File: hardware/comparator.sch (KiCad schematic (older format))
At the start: 16 parts, among them U401 ADCMP580, U402 SY89321L

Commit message: added picture of assembled pcb, started erratum for r0..
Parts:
- R408: value JMP -> DNI
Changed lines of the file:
@@
 P 5700 4500
 F 0 "R408" V 5800 4550 50  0000 L CNN
-F 1 "JMP" V 5800 4350 50  0000 L CNN
+F 1 "DNI" V 5800 4350 50  0000 L CNN
 F 2 "Resistors_SMD:R_0402" H 5700 4500 50  0001 C CNN
 F 3 "~" H 5700 4500 50  0001 C CNN

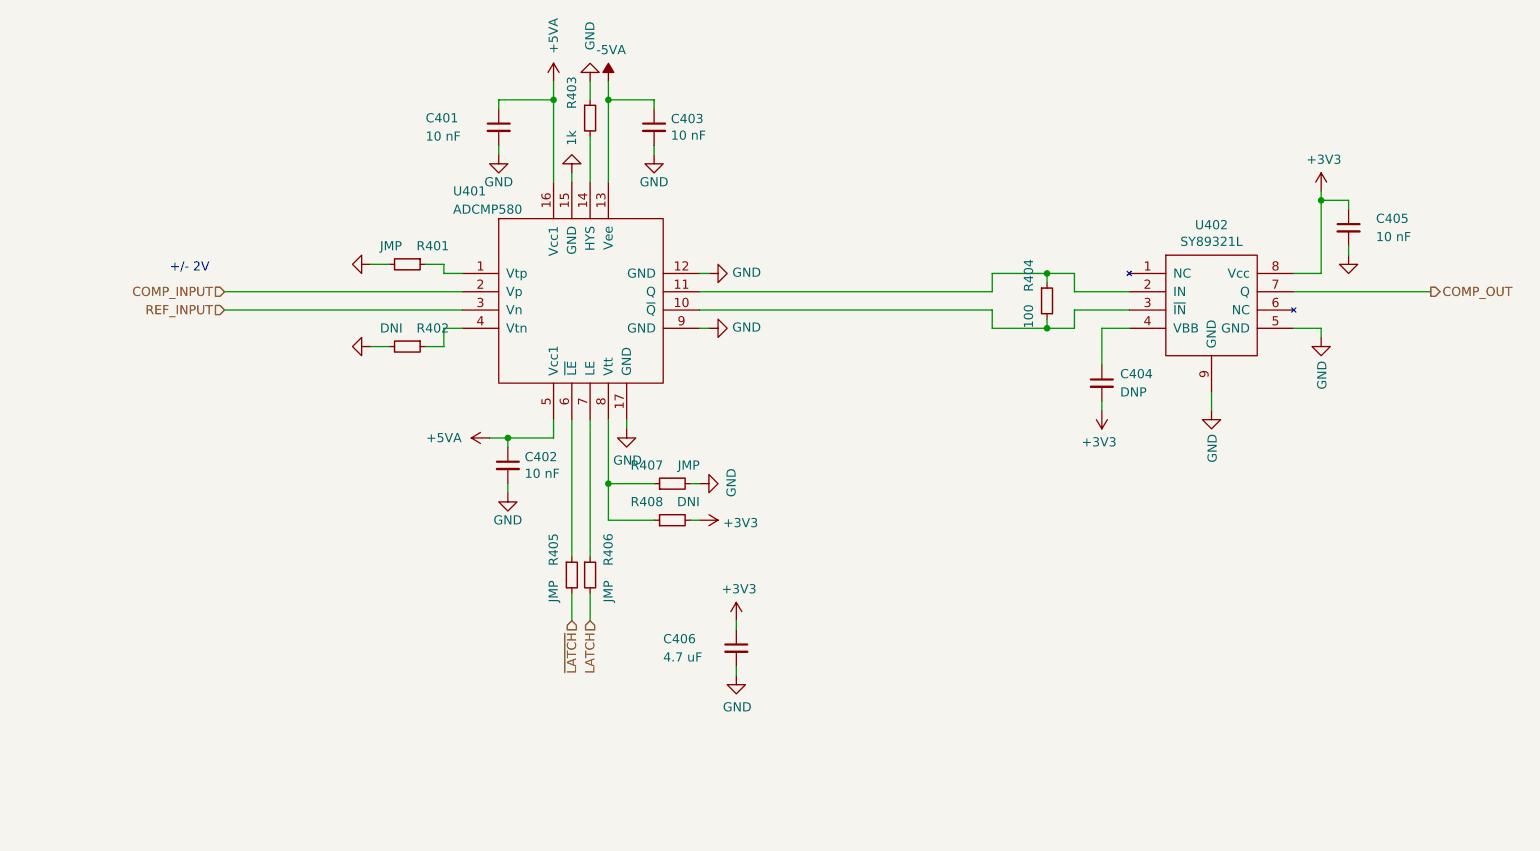
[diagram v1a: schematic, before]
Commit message: fixed U401 and U601 output termination, tdr works, added first sweep of output pulse to README
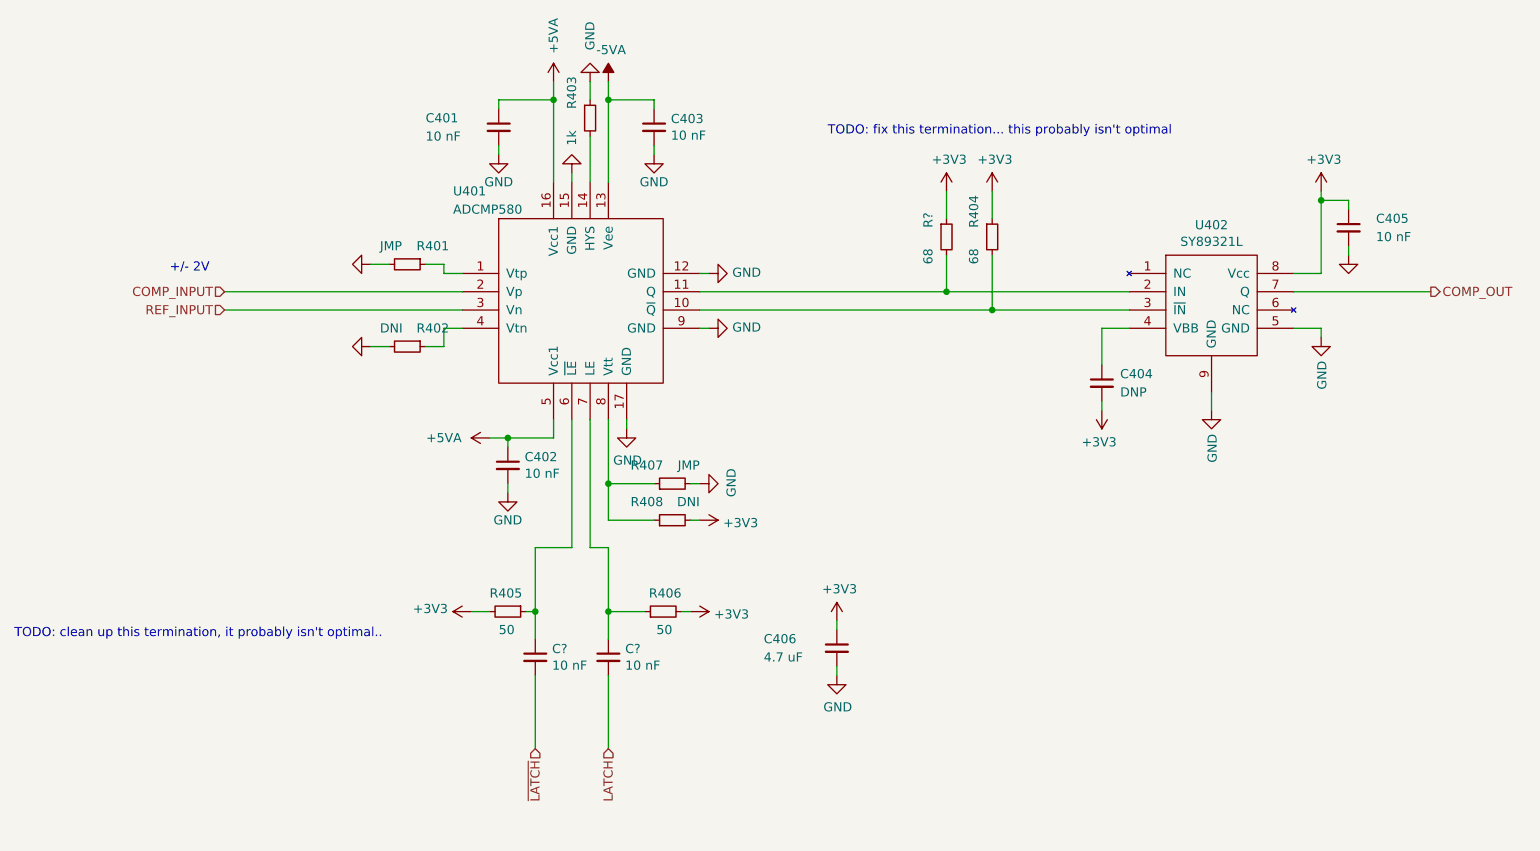
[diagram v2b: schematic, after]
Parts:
- added C? (x2): 10 nF, Capacitors_SMD:C_0402, symbol Device:C_Small
- added R?: 68, Resistors_SMD:R_0402, symbol Device:R_Small
- R404: value 100 -> 68
- R405, R406: value JMP -> 50
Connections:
- net +3V3: now also R404.1, R405.2, R406.2, R?.1
- net LATCH: now also C?.2; no longer R406.2
- net ~LATCH: now also C?.2; no longer R405.2
- net at U401.11 (Q), U402.2 (IN): now also R?.2; no longer R404.1
- net at R405.1, U401.6 (~LE): now also C?.1
- net at R406.1, U401.7 (LE): now also C?.1
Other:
- note added: "TODO: clean up this termination, it probably isn't optimal.."
- note added: "TODO: fix this termination... this probably isn't optimal"
- moved on the sheet: C406, R404, R405, R406
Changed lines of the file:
@@
 Text HLabel 3250 3350 0    50   Input ~ 0
 REF_INPUT
-Text HLabel 5150 5050 3    50   Input ~ 0
+Text HLabel 4950 5750 3    50   Input ~ 0
 ~LATCH
-Text HLabel 5250 5050 3    50   Input ~ 0
+Text HLabel 5350 5750 3    50   Input ~ 0
 LATCH
 $Comp
@@
 L Device:R_Small R404
 U 1 1 5BC3F0C6
-P 7750 3300
-F 0 "R404" V 7650 3350 50  0000 L CNN
-F 1 "100" V 7650 3150 50  0000 L CNN
-F 2 "Resistors_SMD:R_0402" H 7750 3300 50  0001 C CNN
-F 3 "~" H 7750 3300 50  0001 C CNN
-	1    7750 3300
-	1    0    0    -1
-$EndComp
-Wire Wire Line
-	7450 3250 7450 3150
-Wire Wire Line
-	7450 3150 7750 3150
-Wire Wire Line
-	7900 3150 7900 3250
-Wire Wire Line
-	7900 3250 8200 3250
-Wire Wire Line
-	5850 3250 7450 3250
-Wire Wire Line
-	7450 3350 7450 3450
-Wire Wire Line
-	7450 3450 7750 3450
-Wire Wire Line
-	7900 3450 7900 3350
-Wire Wire Line
-	7900 3350 8200 3350
-Wire Wire Line
-	5850 3350 7450 3350
-Wire Wire Line
-	7750 3200 7750 3150
-Connection ~ 7750 3150
-Wire Wire Line
-	7750 3150 7900 3150
-Wire Wire Line
-	7750 3400 7750 3450
-Connection ~ 7750 3450
-Wire Wire Line
-	7750 3450 7900 3450
+P 7450 2950
+F 0 "R404" V 7350 3000 50  0000 L CNN
+F 1 "68" V 7350 2800 50  0000 L CNN
+F 2 "Resistors_SMD:R_0402" H 7450 2950 50  0001 C CNN
+F 3 "~" H 7450 2950 50  0001 C CNN
+	1    7450 2950
+	1    0    0    -1
+$EndComp
 $Comp
 L power:+3V3 #PWR0225
@@
 L Device:R_Small R405
 U 1 1 5C37AFC8
-P 5150 4800
-F 0 "R405" V 5050 4850 50  0000 L CNN
-F 1 "JMP" V 5050 4650 50  0000 L CNN
-F 2 "Resistors_SMD:R_0402" H 5150 4800 50  0001 C CNN
-F 3 "~" H 5150 4800 50  0001 C CNN
-	1    5150 4800
-	1    0    0    -1
+P 4800 5000
+F 0 "R405" V 4700 4900 50  0000 L CNN
+F 1 "50" V 4900 4950 50  0000 L CNN
+F 2 "Resistors_SMD:R_0402" H 4800 5000 50  0001 C CNN
+F 3 "~" H 4800 5000 50  0001 C CNN
+	1    4800 5000
+	0    1    1    0
 $EndComp
 $Comp
 L Device:R_Small R406
 U 1 1 5C37B0A4
-P 5250 4800
-F 0 "R406" V 5350 4850 50  0000 L CNN
-F 1 "JMP" V 5350 4650 50  0000 L CNN
-F 2 "Resistors_SMD:R_0402" H 5250 4800 50  0001 C CNN
-F 3 "~" H 5250 4800 50  0001 C CNN
-	1    5250 4800
-	1    0    0    -1
-$EndComp
-Wire Wire Line
-	5250 3950 5250 4700
-Wire Wire Line
-	5150 3950 5150 4700
-Wire Wire Line
-	5150 4900 5150 5050
-Wire Wire Line
-	5250 4900 5250 5050
+P 5650 5000
+F 0 "R406" V 5750 4900 50  0000 L CNN
+F 1 "50" V 5550 4950 50  0000 L CNN
+F 2 "Resistors_SMD:R_0402" H 5650 5000 50  0001 C CNN
+F 3 "~" H 5650 5000 50  0001 C CNN
+	1    5650 5000
+	0    -1   -1   0
+$EndComp
 $Comp
 L Device:R_Small R407
@@
 L Device:C_Small C406
 U 1 1 5C36E21C
-P 6050 5200
-F 0 "C406" H 5650 5250 50  0000 L CNN
-F 1 "4.7 uF" H 5650 5150 50  0000 L CNN
-F 2 "Capacitors_SMD:C_0603" H 6050 5200 50  0001 C CNN
-F 3 "~" H 6050 5200 50  0001 C CNN
-	1    6050 5200
+P 6600 5200
+F 0 "C406" H 6200 5250 50  0000 L CNN
+F 1 "4.7 uF" H 6200 5150 50  0000 L CNN
+F 2 "Capacitors_SMD:C_0603" H 6600 5200 50  0001 C CNN
+F 3 "~" H 6600 5200 50  0001 C CNN
+	1    6600 5200
 	1    0    0    -1
 $EndComp
@@
 L power:+3V3 #PWR0147
 U 1 1 5C36E2D5
-P 6050 5050
-F 0 "#PWR0147" H 6050 4900 50  0001 C CNN
-F 1 "+3V3" H 6065 5223 50  0000 C CNN
-F 2 "" H 6050 5050 50  0001 C CNN
-F 3 "" H 6050 5050 50  0001 C CNN
-	1    6050 5050
-	1    0    0    -1
-$EndComp
-Wire Wire Line
-	6050 5100 6050 5050
+P 6600 5050
+F 0 "#PWR0147" H 6600 4900 50  0001 C CNN
+F 1 "+3V3" H 6615 5223 50  0000 C CNN
+F 2 "" H 6600 5050 50  0001 C CNN
+F 3 "" H 6600 5050 50  0001 C CNN
+	1    6600 5050
+	1    0    0    -1
+$EndComp
+Wire Wire Line
+	6600 5100 6600 5050
 $Comp
 L power:GND #PWR0148
 U 1 1 5C370836
-P 6050 5350
-F 0 "#PWR0148" H 6050 5100 50  0001 C CNN
-F 1 "GND" H 6055 5177 50  0000 C CNN
-F 2 "" H 6050 5350 50  0001 C CNN
-F 3 "" H 6050 5350 50  0001 C CNN
-	1    6050 5350
-	1    0    0    -1
-$EndComp
-Wire Wire Line
-	6050 5300 6050 5350
+P 6600 5350
+F 0 "#PWR0148" H 6600 5100 50  0001 C CNN
+F 1 "GND" H 6605 5177 50  0000 C CNN
+F 2 "" H 6600 5350 50  0001 C CNN
+F 3 "" H 6600 5350 50  0001 C CNN
+	1    6600 5350
+	1    0    0    -1
+$EndComp
+Wire Wire Line
+	6600 5300 6600 5350
+$Comp
+L Device:R_Small R?
+U 1 1 5C6F135B
+P 7200 2950
+F 0 "R?" V 7100 3000 50  0000 L CNN
+F 1 "68" V 7100 2800 50  0000 L CNN
+F 2 "Resistors_SMD:R_0402" H 7200 2950 50  0001 C CNN
+F 3 "~" H 7200 2950 50  0001 C CNN
+	1    7200 2950
+	1    0    0    -1
+$EndComp
+Wire Wire Line
+	5850 3350 7450 3350
+Wire Wire Line
+	5850 3250 7200 3250
+$Comp
+L power:+3V3 #PWR?
+U 1 1 5C6F3BB4
+P 7200 2700
+F 0 "#PWR?" H 7200 2550 50  0001 C CNN
+F 1 "+3V3" H 7215 2873 50  0000 C CNN
+F 2 "" H 7200 2700 50  0001 C CNN
+F 3 "" H 7200 2700 50  0001 C CNN
+	1    7200 2700
+	1    0    0    -1
+$EndComp
+$Comp
+L power:+3V3 #PWR?
+U 1 1 5C6F3BE1
+P 7450 2700
+F 0 "#PWR?" H 7450 2550 50  0001 C CNN
+F 1 "+3V3" H 7465 2873 50  0000 C CNN
+F 2 "" H 7450 2700 50  0001 C CNN
+F 3 "" H 7450 2700 50  0001 C CNN
+	1    7450 2700
+	1    0    0    -1
+$EndComp
+Wire Wire Line
+	7450 2700 7450 2850
+Wire Wire Line
+	7200 2700 7200 2850
+Wire Wire Line
+	7200 3050 7200 3250
+Connection ~ 7200 3250
+Wire Wire Line
+	7200 3250 8200 3250
+Wire Wire Line
+	7450 3050 7450 3350
+Connection ~ 7450 3350
+Wire Wire Line
+	7450 3350 8200 3350
+Text Notes 6550 2400 0    50   ~ 0
+TODO: fix this termination... this probably isn't optimal
+$Comp
+L Device:C_Small C?
+U 1 1 5C7043F2
+P 4950 5250
+F 0 "C?" H 5042 5296 50  0000 L CNN
+F 1 "10 nF" H 5042 5205 50  0000 L CNN
+F 2 "Capacitors_SMD:C_0402" H 4950 5250 50  0001 C CNN
+F 3 "~" H 4950 5250 50  0001 C CNN
+	1    4950 5250
+	1    0    0    -1
+$EndComp
+$Comp
+L Device:C_Small C?
+U 1 1 5C70444C
+P 5350 5250
+F 0 "C?" H 5442 5296 50  0000 L CNN
+F 1 "10 nF" H 5442 5205 50  0000 L CNN
+F 2 "Capacitors_SMD:C_0402" H 5350 5250 50  0001 C CNN
+F 3 "~" H 5350 5250 50  0001 C CNN
+	1    5350 5250
+	1    0    0    -1
+$EndComp
+Text Notes 2100 5150 0    50   ~ 0
+TODO: clean up this termination, it probably isn't optimal..
+Wire Wire Line
+	4900 5000 4950 5000
+Wire Wire Line
+	5150 3950 5150 4650
+Wire Wire Line
+	5350 5150 5350 5000
+Wire Wire Line
+	5350 5000 5550 5000
+Wire Wire Line
+	4950 5150 4950 5000
+$Comp
+L power:+3V3 #PWR?
+U 1 1 5C710F4A
+P 5800 5000
+F 0 "#PWR?" H 5800 4850 50  0001 C CNN
+F 1 "+3V3" V 5815 5128 50  0000 L CNN
+F 2 "" H 5800 5000 50  0001 C CNN
+F 3 "" H 5800 5000 50  0001 C CNN
+	1    5800 5000
+	0    1    1    0
+$EndComp
+Wire Wire Line
+	5800 5000 5750 5000
+$Comp
+L power:+3V3 #PWR?
+U 1 1 5C7126A3
+P 4600 5000
+F 0 "#PWR?" H 4600 4850 50  0001 C CNN
+F 1 "+3V3" V 4615 5128 50  0000 L CNN
+F 2 "" H 4600 5000 50  0001 C CNN
+F 3 "" H 4600 5000 50  0001 C CNN
+	1    4600 5000
+	0    -1   -1   0
+$EndComp
+Wire Wire Line
+	4600 5000 4700 5000
+Wire Wire Line
+	5350 5350 5350 5750
+Wire Wire Line
+	4950 5000 4950 4650
+Wire Wire Line
+	4950 4650 5150 4650
+Connection ~ 4950 5000
+Connection ~ 5350 5000
+Wire Wire Line
+	5350 5000 5350 4650
+Wire Wire Line
+	5350 4650 5250 4650
+Wire Wire Line
+	5250 4650 5250 3950
+Wire Wire Line
+	4950 5750 4950 5350
 $EndSCHEMATC

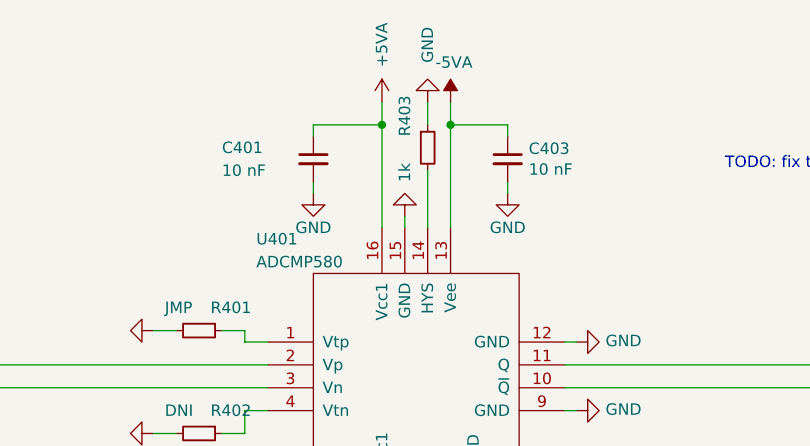
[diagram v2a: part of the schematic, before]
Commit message: fix crossover distortion on analog triggered measurements
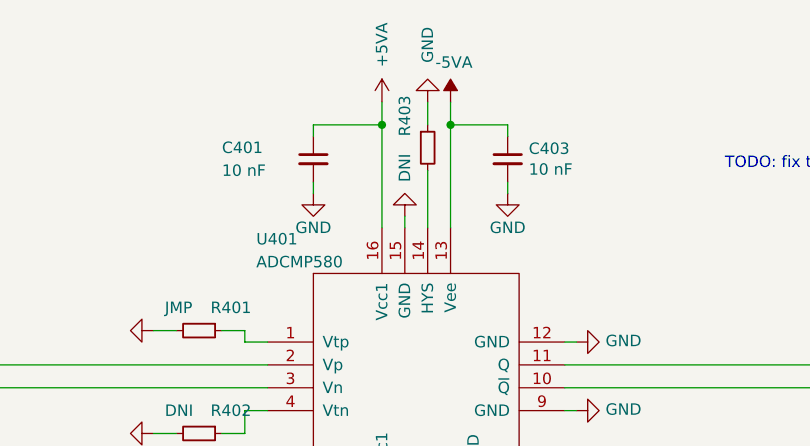
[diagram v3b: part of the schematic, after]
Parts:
- R403: value 1k -> DNI
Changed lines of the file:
@@
 P 5250 2300
 F 0 "R403" V 5150 2350 50  0000 L CNN
-F 1 "1k" V 5150 2150 50  0000 L CNN
+F 1 "DNI" V 5150 2150 50  0000 L CNN
 F 2 "Resistors_SMD:R_0402" H 5250 2300 50  0001 C CNN
 F 3 "~" H 5250 2300 50  0001 C CNN
